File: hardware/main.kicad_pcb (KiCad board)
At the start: 4 copper layers, 57 x 93 mm, 430 parts, among them J1 DS1128-09-S8B8X, J10 AS0BC21-S30BM-7H, J2 DS1128-09-S8B8X, J3 DS1128-09-S8B8X, J4 98424-G52-04ALF, J5 miniPCI-E_52P_5.2, J6 1042240820, J8 USB_C_Receptacle, J9 TYPE-C-31-M-12, Q1 SSM6J501NU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

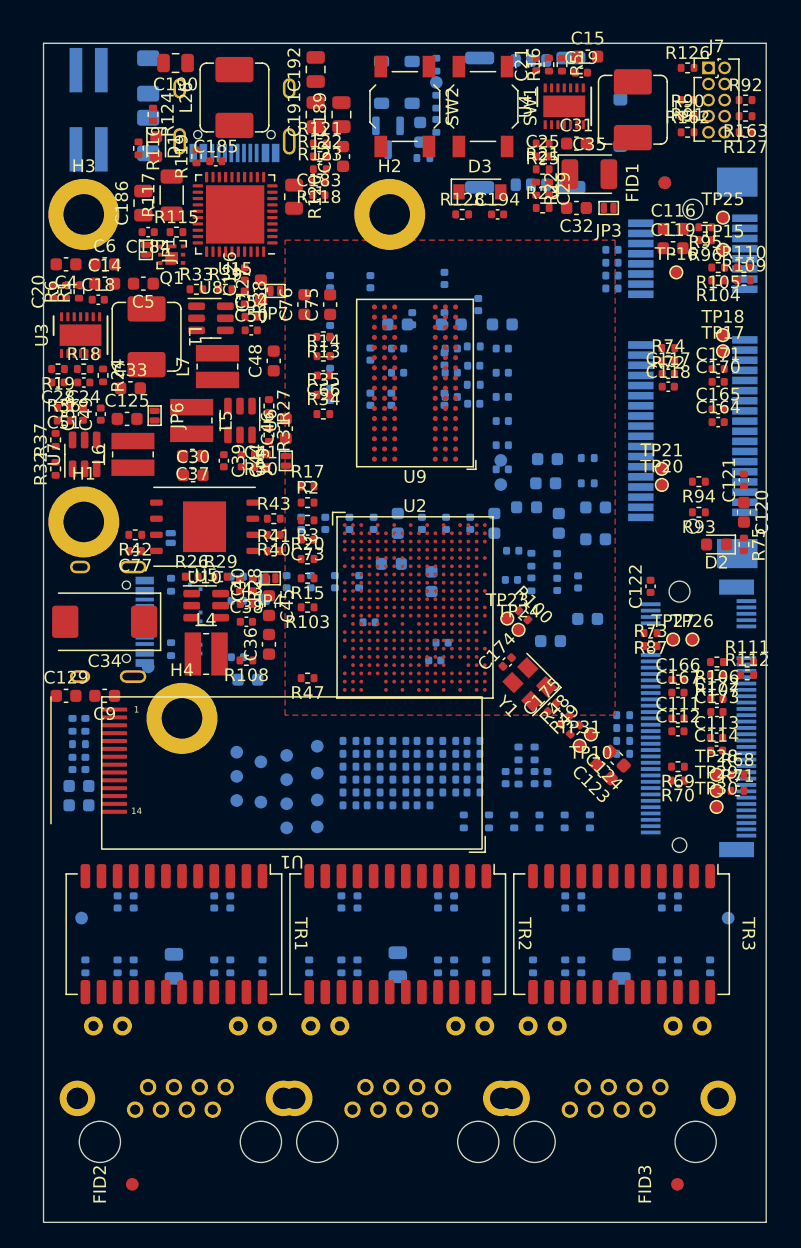
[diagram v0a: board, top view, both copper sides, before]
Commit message: update outline
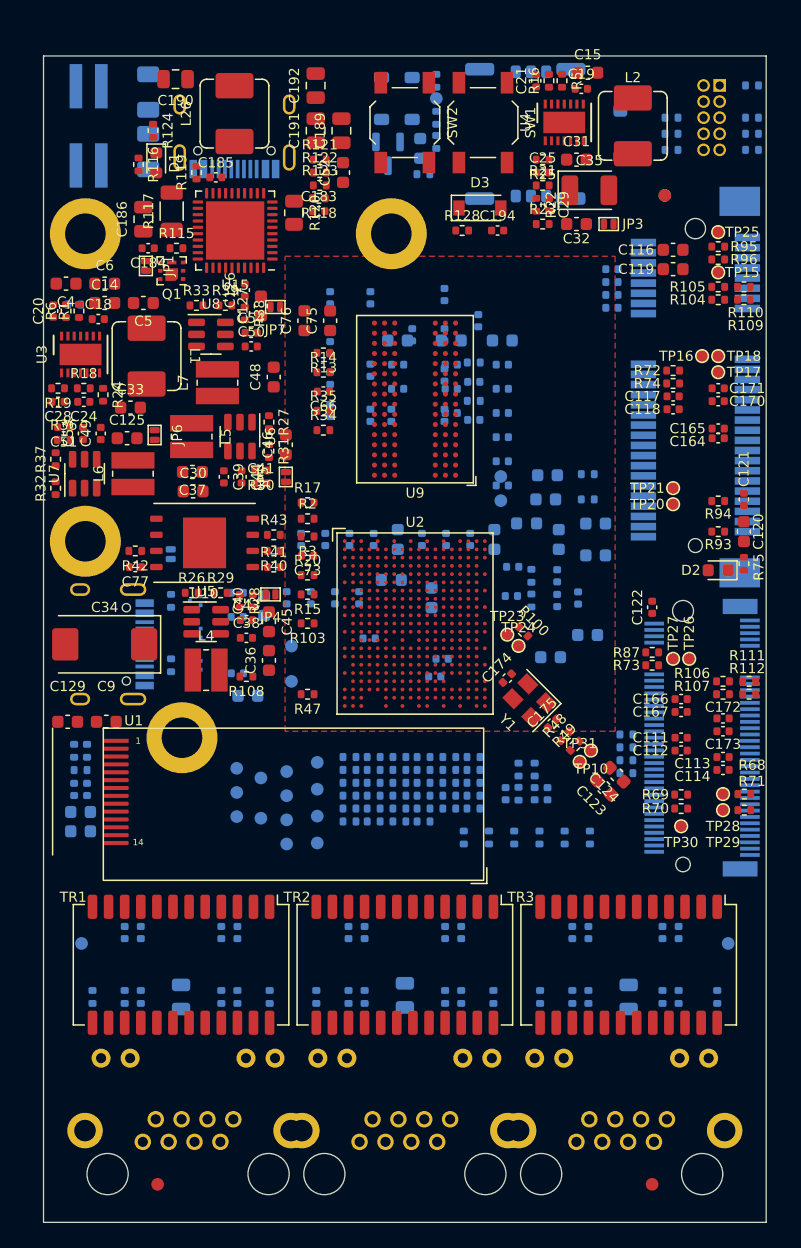
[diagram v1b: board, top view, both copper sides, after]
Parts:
- J7, R126, R127, R162, R163, R90, R91, R92: moved to B.Cu
- moved TP11 11.4 mm to (19.6, -42.7)
- moved TP12 11.4 mm to (19.6, -45.5)
- moved TP16 6.91 mm to (51.9, -68.3)
- moved R127 6.00 mm to (49.5, -84.6), turned to 0 degrees
- moved R163 6.00 mm to (49.5, -85.9), turned to 0 degrees
- moved R92 6.00 mm to (49.5, -87.1), turned to 180 degrees
- moved R126 5.27 mm to (55.9, -89.7), turned to 180 degrees
- moved R162 5.27 mm to (55.9, -84.6), turned to 180 degrees
- moved R90 5.27 mm to (55.9, -85.9), turned to 180 degrees
- moved R91 5.27 mm to (55.9, -87.1), turned to 0 degrees
- moved TP30 3.18 mm to (50.3, -31.2)
- moved J1 2.61 mm to (7.83, -6.35)
- moved J2 2.60 mm to (24.9, -6.35)
- moved J3 2.59 mm to (42.0, -6.35)
- moved C100 2.48 mm to (31.7, -22.9)
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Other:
- board size 57 x 93 mm -> 57 x 92 mm

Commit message: update pcb
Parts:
- C1, C105, C107, C108, C162, C17, C23, C47, C7, C81, C82, JP2, R4: moved to F.Cu
- C33, C52: moved to B.Cu
- J8: footprint Connector_USB:USB_C_Receptacle_HRO_TYPE-C-31-M-12 -> MAS_Package_std:HRS_CX90B1-24P
- moved C12 87.1 mm to (112.8, -47.8)
- moved C8 87.1 mm to (112.8, -45.9)
- moved R108 77.1 mm to (93.1, -44.5)
- moved C115 74.8 mm to (113.0, -43.7)
- moved C104 72.4 mm to (88.9, -18.0)
- moved C106 72.4 mm to (87.0, -18.0)
- moved C109 72.4 mm to (85.1, -18.0)
- moved C110 72.4 mm to (83.2, -18.0)
- moved C102 72.4 mm to (92.7, -18.0)
- moved C87 72.4 mm to (96.5, -18.0)
- moved C93 72.4 mm to (94.6, -18.0)
- moved C10 67.3 mm to (103.3, -72.8)
- moved C13 67.3 mm to (103.3, -70.9)
- moved C22 67.3 mm to (103.3, -69.0)
- moved C26 67.3 mm to (103.3, -67.1)
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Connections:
- C33 pad 1: Net-(JP2-B) -> +5V
- J10 pad S1: (no net) -> -BATT
- J10 pad S2: (no net) -> -BATT
- J6 pad N.C.: (no net) -> unconnected-(J6-PadN.C.)
- U14 pad 1: /SSUSB_TXP -> Net-(J8-TX1+)
- U14 pad 2: /SSUSB_TXN -> Net-(J8-TX1-)

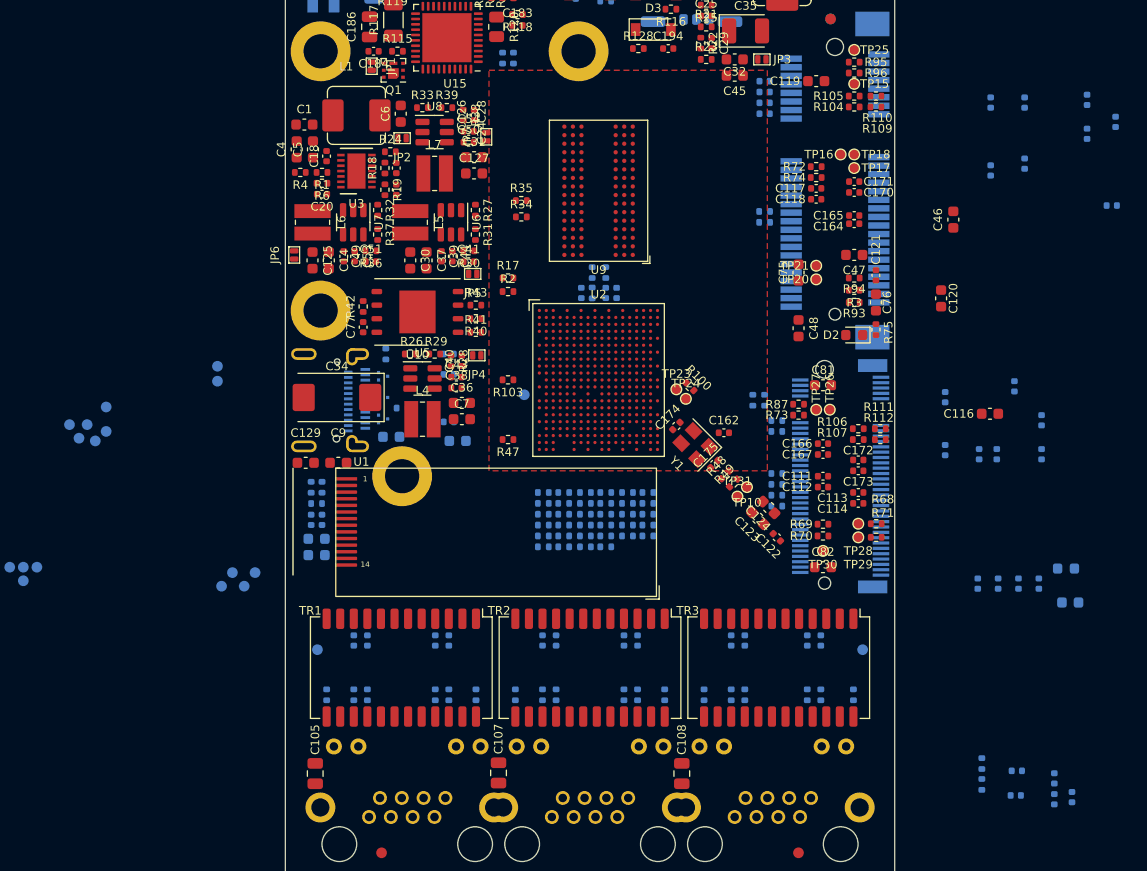
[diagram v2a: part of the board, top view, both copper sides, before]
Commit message: updated rules for differential pairs
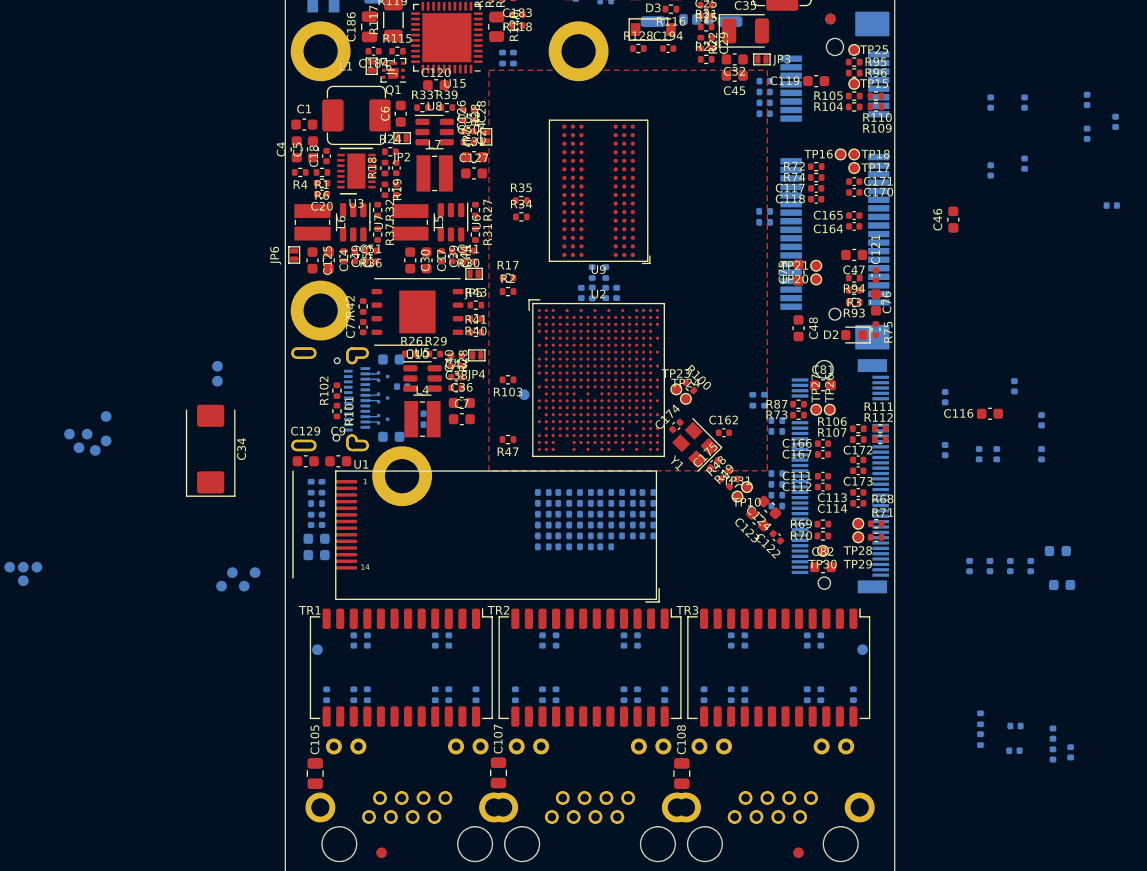
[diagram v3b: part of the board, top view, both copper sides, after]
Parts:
- R101, R102: moved to F.Cu
- moved C120 51.3 mm to (14.1, -74.8), turned to 0 degrees
- moved C34 12.8 mm to (-6.99, -40.8), turned to 90 degrees
- moved C139 9.83 mm to (9.91, -49.1), turned to 0 degrees
- moved C160 7.19 mm to (12.4, -43.1)
- moved R101 6.10 mm to (4.83, -44.3), turned to -90 degrees
- moved R102 5.71 mm to (4.83, -46.2)
- moved C161 5.47 mm to (10.9, -46.6)
- moved C159 4.65 mm to (12.4, -44.1)
- moved C141 4.19 mm to (68.2, -12.6)
- moved C169 4.19 mm to (71.8, -12.2)
- moved C178 4.19 mm to (71.8, -14.1)
- moved C55 4.19 mm to (68.3, -14.9)
- moved R113 4.19 mm to (65.0, -15.5)
- moved R114 4.19 mm to (65.0, -13.6)
- moved C56 4.19 mm to (73.5, -12.4)
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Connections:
- net /ESW_TXVN_A_P2 renamed /ESW_A_P2_TXVN
- net /ESW_TXVN_A_P3 renamed /ESW_A_P3_TXVN
- net /ESW_TXVN_A_P4 renamed /ESW_A_P4_TXVN
- net /ESW_TXVN_B_P2 renamed /ESW_B_P2_TXVN
- net /ESW_TXVN_B_P3 renamed /ESW_B_P3_TXVN
- net /ESW_TXVN_B_P4 renamed /ESW_B_P4_TXVN
- net /ESW_TXVN_C_P2 renamed /ESW_C_P2_TXVN
- net /ESW_TXVN_C_P3 renamed /ESW_C_P3_TXVN
- net /ESW_TXVN_C_P4 renamed /ESW_C_P4_TXVN
- net /ESW_TXVN_D_P2 renamed /ESW_D_P2_TXVN
- net /ESW_TXVN_D_P3 renamed /ESW_D_P3_TXVN
- net /ESW_TXVN_D_P4 renamed /ESW_D_P4_TXVN
- net /ESW_TXVP_A_P2 renamed /ESW_A_P2_TXVP
- net /ESW_TXVP_A_P3 renamed /ESW_A_P3_TXVP
- net /ESW_TXVP_A_P4 renamed /ESW_A_P4_TXVP
- net /ESW_TXVP_B_P2 renamed /ESW_B_P2_TXVP
- net /ESW_TXVP_B_P3 renamed /ESW_B_P3_TXVP
- net /ESW_TXVP_B_P4 renamed /ESW_B_P4_TXVP
- net /ESW_TXVP_C_P2 renamed /ESW_C_P2_TXVP
- net /ESW_TXVP_C_P3 renamed /ESW_C_P3_TXVP
- net /ESW_TXVP_C_P4 renamed /ESW_C_P4_TXVP
- net /ESW_TXVP_D_P2 renamed /ESW_D_P2_TXVP
- net /ESW_TXVP_D_P3 renamed /ESW_D_P3_TXVP
- net /ESW_TXVP_D_P4 renamed /ESW_D_P4_TXVP
- net /RCLK renamed /RCLK_P
- net /RDQS0 renamed /RDQS0_P
- net /RDQS1 renamed /RDQS1_P
- net /USB_DM renamed /USB_DN
- net /~{RCLK} renamed /RCLK_N
- net /~{RDQS0} renamed /RDQS0_N
- net /~{RDQS1} renamed /RDQS1_N
- net Net-(J8-TX1+) renamed /_SSUSB_TXP
- net Net-(J8-TX1-) renamed /_SSUSB_TXN
- net Net-(U2B-PCIE_CKN0) renamed /_PCIE_CK1_N
- net Net-(U2B-PCIE_CKN1) renamed /_PCIE_CK0_N
- net Net-(U2B-PCIE_CKN2) renamed /_PCIE_CK2_N
- net Net-(U2B-PCIE_CKP0) renamed /_PCIE_CK1_P
- net Net-(U2B-PCIE_CKP1) renamed /_PCIE_CK0_P
- net Net-(U2B-PCIE_CKP2) renamed /_PCIE_CK2_P
- net Net-(U2B-PCIE_RXN0) renamed /_PCIE_RX1_N
- net Net-(U2B-PCIE_RXN1) renamed /_PCIE_RX0_N
- net Net-(U2B-PCIE_RXN2) renamed /_PCIE_RX2_N
- net Net-(U2B-PCIE_RXP0) renamed /_PCIE_RX1_P
- net Net-(U2B-PCIE_RXP1) renamed /_PCIE_RX0_P
- net Net-(U2B-PCIE_RXP2) renamed /_PCIE_RX2_P
- net Net-(U2B-PCIE_TXN0) renamed /_PCIE_TX1_N
- net Net-(U2B-PCIE_TXN1) renamed /_PCIE_TX0_N
- net Net-(U2B-PCIE_TXN2) renamed /_PCIE_TX2_N
- net Net-(U2B-PCIE_TXP0) renamed /_PCIE_TX1_P
- net Net-(U2B-PCIE_TXP1) renamed /_PCIE_TX0_P
- net Net-(U2B-PCIE_TXP2) renamed /_PCIE_TX2_P
- U13 pad 1: /SSUSB_RXP -> /SSUSB_RXN
- U13 pad 2: /SSUSB_RXN -> /SSUSB_RXP
- U2 pad K1: /USB1_DM -> /USB1_DN
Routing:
- net /_SSUSB_TXN: track 0.00 -> 1.28 mm
- net /USB_DN: track 0.00 -> 1.28 mm
- net /SSUSB_RXP: track 0.00 -> 1.28 mm
- net /_SSUSB_TXP: track 0.00 -> 1.28 mm
- net /USB_DP: track 0.00 -> 1.28 mm
- net /SSUSB_RXN: track 0.00 -> 1.28 mm

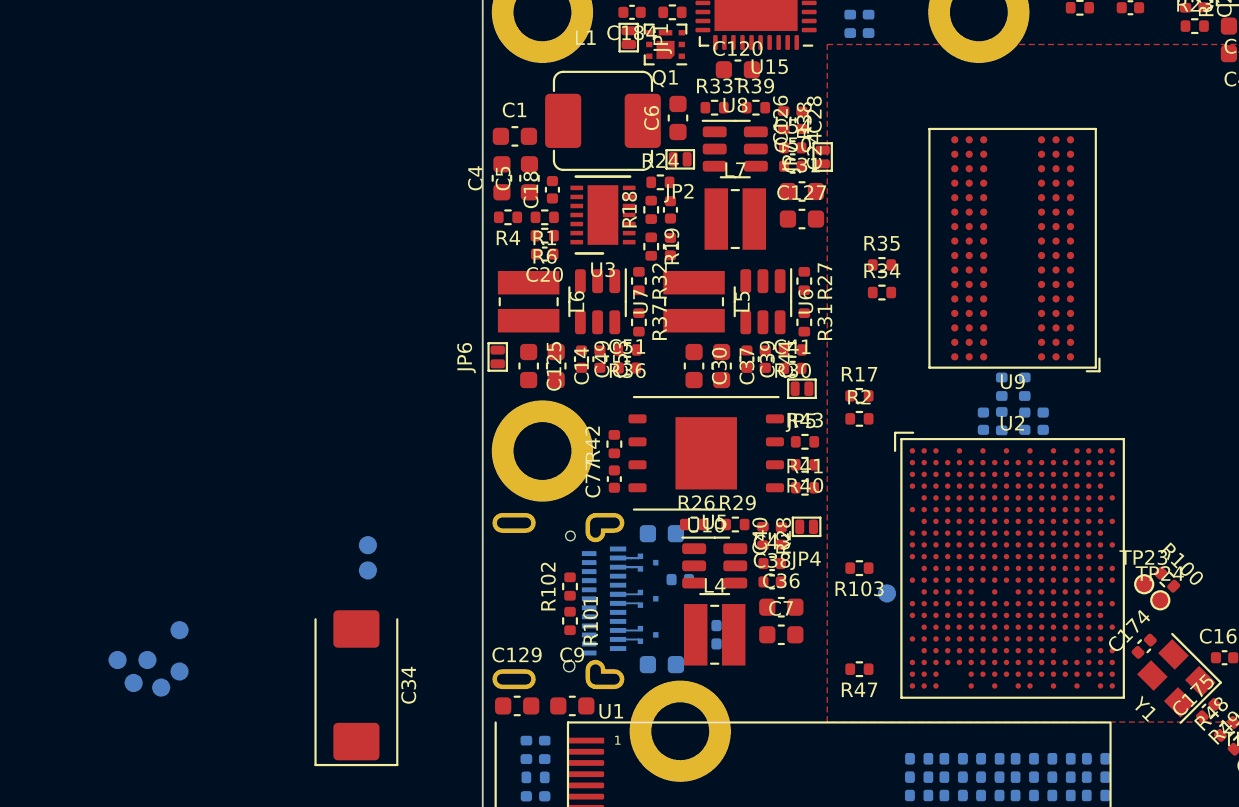
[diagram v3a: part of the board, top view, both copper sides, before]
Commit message: calc Impedance and mark wire
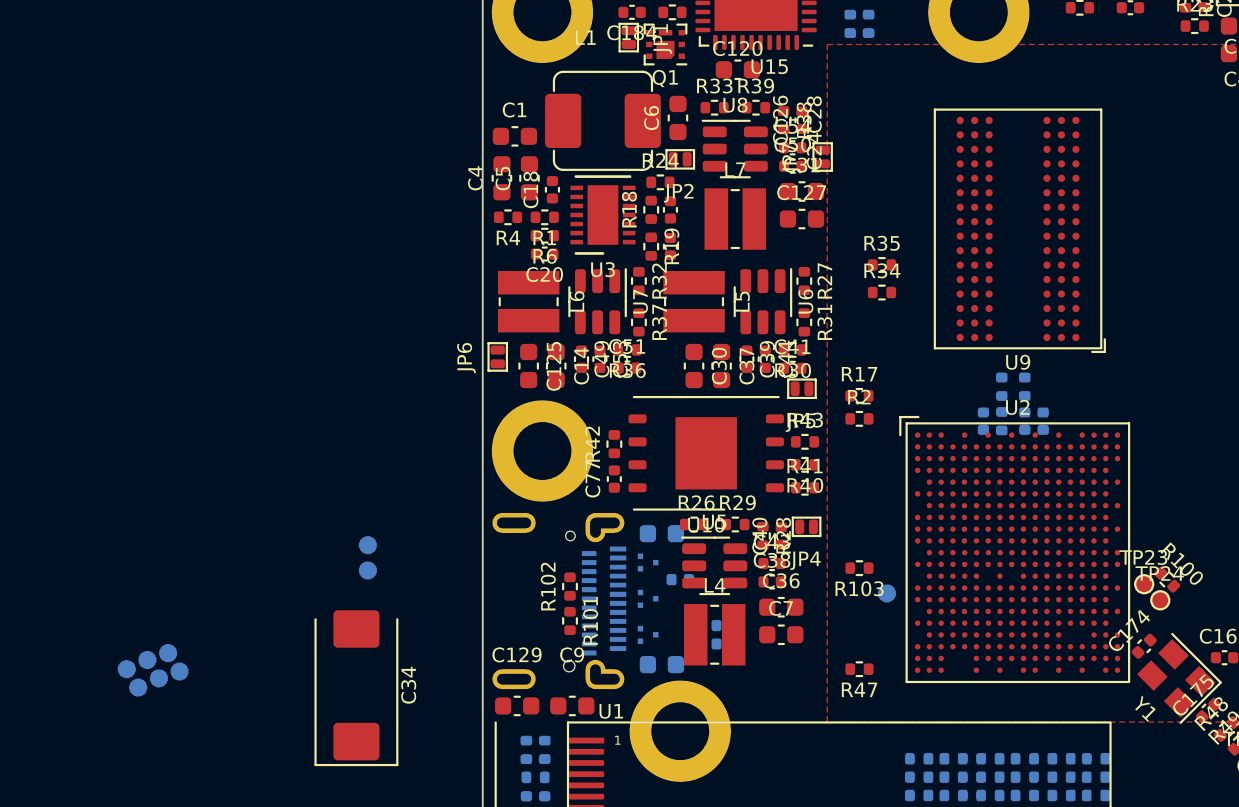
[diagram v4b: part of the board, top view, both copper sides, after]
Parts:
- moved TP9 1.42 mm to (-17.4, -42.5)
- moved U9 1.11 mm to (29.6, -66.0)
- moved U2 0.92 mm to (29.6, -48.1)
- moved TP6 0.72 mm to (-19.7, -41.7)
- moved TP7 0.52 mm to (-17.9, -41.1)
- moved TP8 0.36 mm to (-19.1, -40.6)
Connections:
- net /DDR3RSTB renamed /DDR_STB
- net /ND_CS_N renamed /SPI_CS_N
- net /ND_D4 renamed /SPI_D4
- net /ND_D5 renamed /SPI_D5
- net /ND_D6 renamed /SPI_D6
- net /ND_D7 renamed /SPI_D7
- net /ND_RE_N renamed /SPI_RE_N
- net /ND_WE_N renamed /SPI_WE_N
- net /P2A_N renamed /ESW_P2A_N
- net /P2A_P renamed /ESW_P2A_P
- net /P2B_N renamed /ESW_P2B_N
- net /P2B_P renamed /ESW_P2B_P
- net /P2C_N renamed /ESW_P2C_N
- net /P2C_P renamed /ESW_P2C_P
- net /P2D_N renamed /ESW_P2D_N
- net /P2D_P renamed /ESW_P2D_P
- net /P3A_N renamed /ESW_P3A_N
- net /P3A_P renamed /ESW_P3A_P
- net /P3B_N renamed /ESW_P3B_N
- net /P3B_P renamed /ESW_P3B_P
- net /P3C_N renamed /ESW_P3C_N
- net /P3C_P renamed /ESW_P3C_P
- net /P3D_N renamed /ESW_P3D_N
- net /P3D_P renamed /ESW_P3D_P
- net /P4A_N renamed /ESW_P4A_N
- net /P4A_P renamed /ESW_P4A_P
- net /P4B_N renamed /ESW_P4B_N
- net /P4B_P renamed /ESW_P4B_P
- net /P4C_N renamed /ESW_P4C_N
- net /P4C_P renamed /ESW_P4C_P
- net /P4D_N renamed /ESW_P4D_N
- net /P4D_P renamed /ESW_P4D_P
- net /RA0 renamed /DDR_A0
- net /RA1 renamed /DDR_A1
- net /RA10 renamed /DDR_A10
- net /RA11 renamed /DDR_A11
- net /RA12 renamed /DDR_A12
- net /RA13 renamed /DDR_A13
- net /RA14 renamed /DDR_A14
- net /RA2 renamed /DDR_A2
- net /RA3 renamed /DDR_A3
- net /RA4 renamed /DDR_A4
- net /RA5 renamed /DDR_A5
- net /RA6 renamed /DDR_A6
- net /RA7 renamed /DDR_A7
- net /RA8 renamed /DDR_A8
- net /RA9 renamed /DDR_A9
- net /RBA0 renamed /DDR_BA0
- net /RBA1 renamed /DDR_BA1
- net /RBA2 renamed /DDR_BA2
- net /RCKE renamed /DDR_CKE
- net /RCLK_N renamed /DDR_CLK_N
- net /RCLK_P renamed /DDR_CLK_P
- net /RDQ0 renamed /DDR_Q0
- net /RDQ1 renamed /DDR_Q1
- net /RDQ10 renamed /DDR_Q10
- net /RDQ11 renamed /DDR_Q11
- net /RDQ12 renamed /DDR_Q12
- net /RDQ13 renamed /DDR_Q13
- net /RDQ14 renamed /DDR_Q14
- net /RDQ15 renamed /DDR_Q15
- net /RDQ2 renamed /DDR_Q2
- net /RDQ3 renamed /DDR_Q3
- net /RDQ4 renamed /DDR_Q4
- net /RDQ5 renamed /DDR_Q5
- net /RDQ6 renamed /DDR_Q6
- net /RDQ7 renamed /DDR_Q7
- net /RDQ8 renamed /DDR_Q8
- net /RDQ9 renamed /DDR_Q9
- net /RDQM0 renamed /DDR_QM0
- net /RDQM1 renamed /DDR_QM1
- net /RDQS0_N renamed /DDR_QS0_N
- net /RDQS0_P renamed /DDR_QS0_P
- net /RDQS1_N renamed /DDR_QS1_N
- net /RDQS1_P renamed /DDR_QS1_P
- net /RODT renamed /DDR_ODT
- net /SSUSB_RXN renamed /USB_RXN
- net /SSUSB_RXP renamed /USB_RXP
- net /SSUSB_TXN renamed /USB_TXN
- net /SSUSB_TXP renamed /USB_TXP
- net /_SSUSB_TXN renamed /_USB_TXN
- net /_SSUSB_TXP renamed /_USB_TXP
- net /~{RCAS} renamed /DDR_~{CAS}
- net /~{RCS} renamed /DDR_~{CS}
- net /~{RRAS} renamed /DDR_~{RAS}
- net /~{RWE} renamed /DDR_~{WE}
- net Net-(J7-Pin_1) renamed /JTCLK
- net Net-(J7-Pin_10) renamed /JTMS
- net Net-(J7-Pin_7) renamed /JTRST_N
- net Net-(J7-Pin_8) renamed /JTDI
- net Net-(J7-Pin_9) renamed /JTDO
- J5 pad 36: /USB1_DM -> /USB1_DN
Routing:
- net /_USB_TXN: track 1.28 -> 0.00 mm
- net /USB_DN: track 1.28 -> 0.00 mm
- net /USB_RXP: track 1.28 -> 0.00 mm
- net /_USB_TXP: track 1.28 -> 0.00 mm
- net /USB_RXN: track 1.28 -> 0.00 mm
- net /USB_DP: track 1.28 -> 0.00 mm
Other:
- copper layers 4 -> 6
